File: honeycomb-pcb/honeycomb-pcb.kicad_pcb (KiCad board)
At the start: 4 copper layers, 40 x 40 mm, 103 parts, among them J1301 Connector_USB_C_Receptacle, J301 Molex_Pico-SPOX_Horizontal, J302 Molex_Pico-Lock-PLUS_Vertical, J401 Molex_Pico-SPOX_Horizontal, J402 Molex_Pico-Clasp_Horizontal, M301 Fan_5VDC_25x25x8mm, Q301 MOSFET-N-CH, SW1301 Switch_Tactile_SPST-NO_SMT_Si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, U1001 BUK7D36-60EX, U1101 BUK7D36-60EX, U1201 BUK7D36-60EX, U1301 Linear_3.3V_1A, U1302 MCU_RP2040, U1303 Memory_Flash_W25Q128JVZPIQ, U301 Switching_5V_500mA, U302 Linear_3.3V_1A, U401 TMC5160A-WA, U402 MAX6816, U501 BUK7D36-60EX, U601 BUK7D36-60EX, U701 BUK7D36-60EX, U801 BUK7D36-60EX, U901 BUK7D36-60EX, X401 16MHz, Y1301 Crystal_12MHz

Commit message: tmc5130-uart-multiplexer -> honeycomb-pcb
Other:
- board text added: "honeycomb-pcb v1.0 2024/05 48V 1.6A RMS 2.2A PEAK"
- board text added: "https://github.com/janelia-kicad/honeycomb-pcb"
- board text removed: "https://github.com/janelia-kicad/tmc5130-uart-multiplexer"
- board text removed: "tmc5130-uart-multiplexer v1.0 2024/05 48V 1.6A RMS 2.2A PEAK"
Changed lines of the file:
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@@
   (paper "A4")
   (title_block
-    (title "tmc5130-uart-multiplexer")
+    (title "honeycomb-pcb")
     (date "2024-05-08")
     (rev "1.0")
@@
     (effects (font (size 1 0.6) (thickness 0.15) bold))
   )
-  (gr_text "tmc5130-uart-multiplexer\nv1.0 2024/05\n48V 1.6A RMS 2.2A PEAK" (at 158.4 116.1) (layer "F.SilkS")
+  (gr_text "honeycomb-pcb\nv1.0 2024/05\n48V 1.6A RMS 2.2A PEAK" (at 158.4 116.1) (layer "F.SilkS")
     (effects (font (size 1 0.6) (thickness 0.15) bold))
   )
-  (gr_text "https://github.com/janelia-kicad/tmc5130-uart-multiplexer" (at 152.4 119.6) (layer "F.SilkS")
+  (gr_text "https://github.com/janelia-kicad/honeycomb-pcb" (at 152.4 119.6) (layer "F.SilkS")
     (effects (font (size 1 0.6) (thickness 0.15) bold))
   )

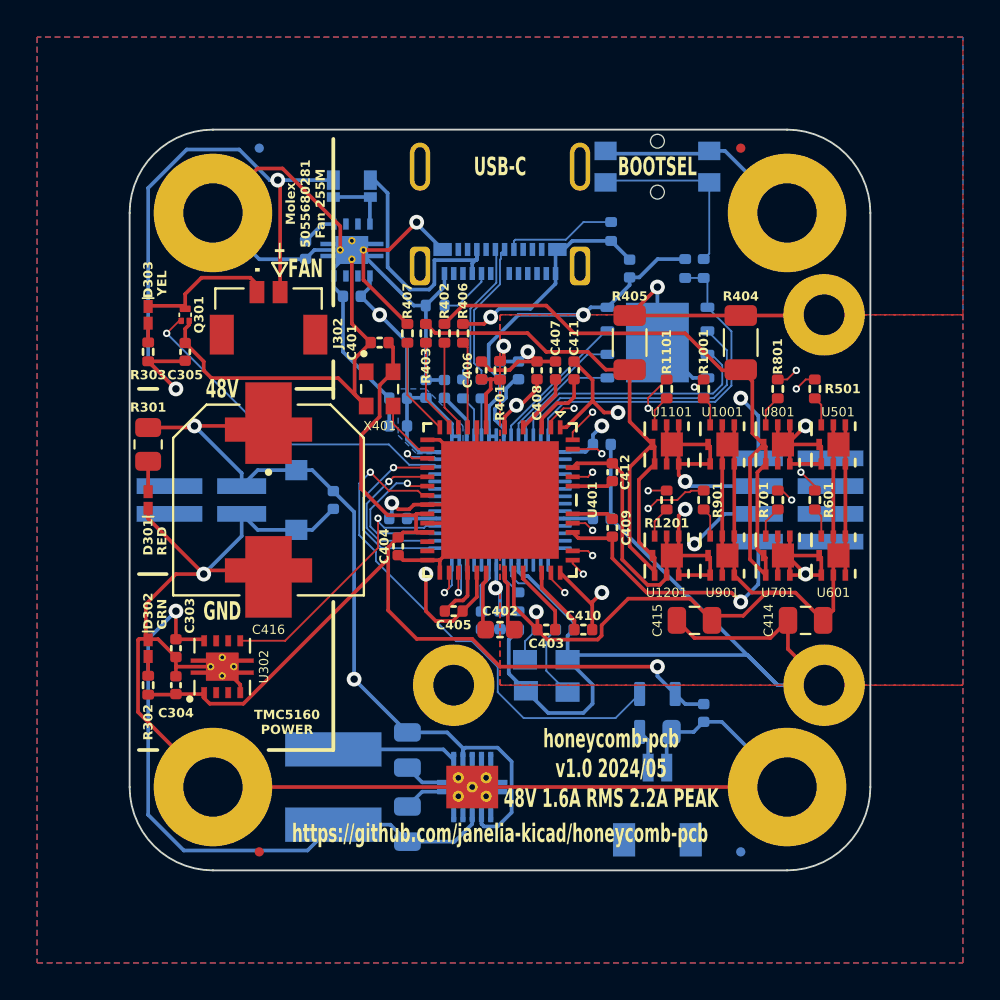
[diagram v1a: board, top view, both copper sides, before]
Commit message: motor -> prism
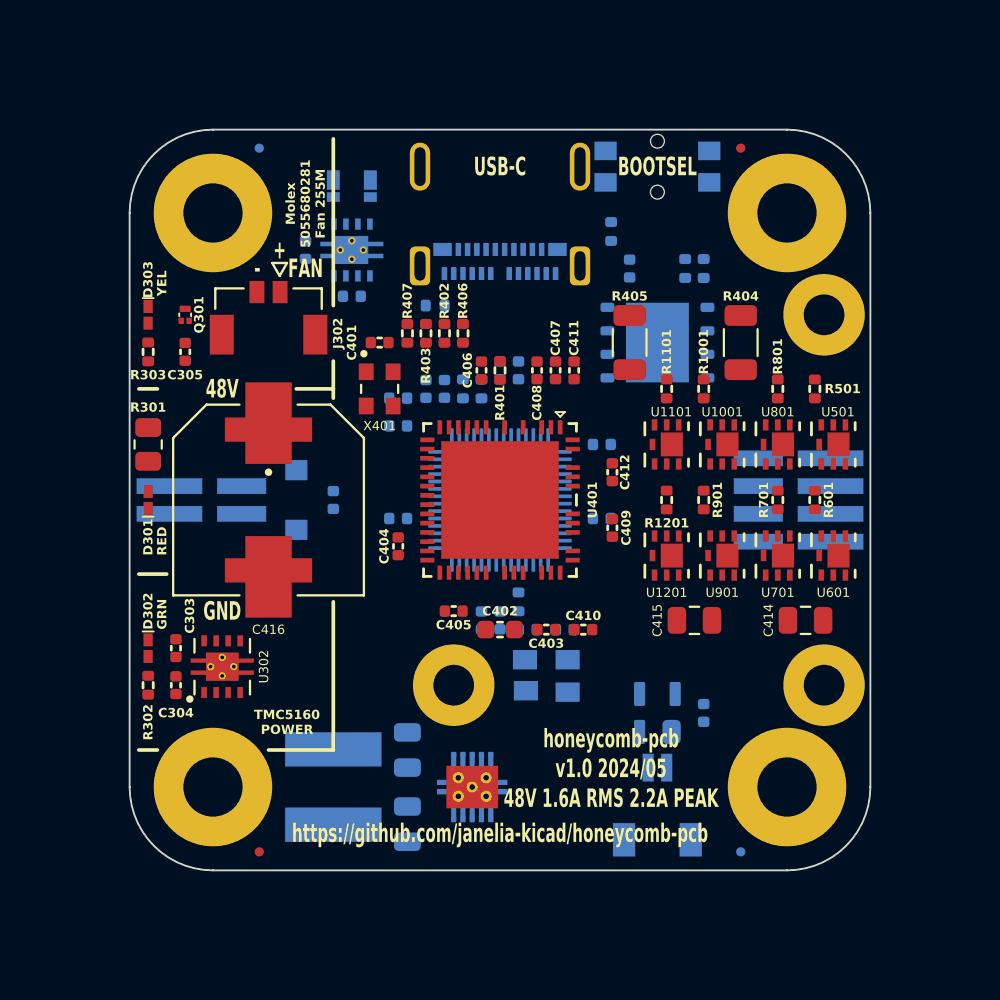
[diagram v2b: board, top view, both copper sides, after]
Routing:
- net /GND: track 474.9 -> 0.00 mm, vias 6 -> 0
- net /VM: track 133.3 -> 0.00 mm, vias 4 -> 0
- net /rp2040/+3.3V: track 87.1 -> 0.00 mm, vias 4 -> 0
- net /+5V: track 81.3 -> 0.00 mm, vias 3 -> 0
- net /VIO: track 56.5 -> 0.00 mm, vias 1 -> 0
- net /tmc5160/BMA1: track 39.3 -> 0.00 mm, vias 2 -> 0
- net /tmc5160/SRA: track 37.6 -> 0.00 mm
- net /tmc5160/BMB2: track 33.1 -> 0.00 mm, vias 2 -> 0
- net /tmc5160/BMA2: track 32.7 -> 0.00 mm, vias 3 -> 0
- net /tmc5160/SRB: track 32.5 -> 0.00 mm
- net /tmc5160/REFL_DEBOUNCED: track 28.1 -> 0.00 mm, vias 1 -> 0
- net /tmc5160/BMB1: track 27.4 -> 0.00 mm, vias 2 -> 0
- net /tmc5160/VCC: track 21.8 -> 0.00 mm, vias 2 -> 0
- net /rp2040/+1.1V: track 20.7 -> 0.00 mm
- net /tmc5160/LA1: track 20.6 -> 0.00 mm, vias 2 -> 0
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- removed copper zone on B.Cu, net /GND
- removed copper zone on F.Cu, net /GND
- removed copper zone on In1.Cu, net /GND
- removed copper zone on F.Cu, net /VM
- removed copper zone on In2.Cu, net /VM
- removed copper zone on B.Cu, net /rp2040/+1.1V
- removed copper zone on B.Cu, net /rp2040/+3.3V

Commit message: Last update before renaming
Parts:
- removed C1301, C1302, C305: 1uF_25V, Janelia:C_0402_1005Metric
- removed C1303, C1311: 1uF_35V, Janelia:C_0402_1005Metric
- removed C1304, C1305, C1306, C1307, C1308, C1309, C1310, C1312, C1313, C1314, C401, C403, C404, C408, C413, C417: 0.1uF_100V, Janelia:C_0402_1005Metric
- removed C1315, C1316: 15pF_25V, Janelia:C_0402_1005Metric
- removed C402: 22nF_100V, Janelia:C_0603_1608Metric
- removed C405: 0.47uF_35V, Janelia:C_0402_1005Metric
- removed C406, C407: 2.2uF_35V, Janelia:C_0402_1005Metric
- removed C409, C410, C411, C412: 0.22uF_25V, Janelia:C_0402_1005Metric
- removed C414, C415: 2.2uF_100V, Janelia:C_0805_2012Metric
- removed C416: 220uF_63V, Janelia:CP_Hybrid_EEHZS1H221V
- removed D1301, D1302: D_SCHOTTKY_40V_2A, Janelia:CR_DSN2_152AB-C_OSI
- removed D302: LED_GRN, Janelia:LED_0402-1005_KNB
- removed D303: LED_YEL, Janelia:LED_0402-1005_KNB
- removed J1301: Connector_USB_C_Receptacle, Janelia:USB_C_Receptacle_Amphenol_10152803-00011LF
- removed J301: Molex_Pico-SPOX_Horizontal, Janelia:Molex_Pico-SPOX-87438_1x02-P1.5mm_Horizontal
- removed J302: Molex_Pico-Lock-PLUS_Vertical, Janelia:Molex_Micro-Lock-PLUS-505568_1x02_P1.25mm_Vertical
- removed J401: Molex_Pico-SPOX_Horizontal, Janelia:Molex_Pico-SPOX-87438_1x04-P1.5mm_Horizontal
- removed J402: Molex_Pico-Clasp_Horizontal, Janelia:Molex_Pico-Clasp-501568_1x02_P1mm_Horizontal
- removed L301: 150uH_553mA, Janelia:IND_CB_SD25
- removed R1201: 15, Janelia:R_0402_1005Metric
- removed R1301: 10.0k, Janelia:R_0402_1005Metric
- removed R1302, R1303: 5.1k, Janelia:R_0402_1005Metric
- removed R1304, R1305: 27, Janelia:R_0402_1005Metric
- removed R1306, R1307: 1k, Janelia:R_0402_1005Metric
- removed R303: 249, Janelia:R_0402_1005Metric
- removed R401: 2.2, Janelia:R_0402_1005Metric
- removed R402, R403, R406, R407: 47, Janelia:R_0402_1005Metric
- removed R404, R405: 0.15, Janelia:R_1206_3216Metric
- removed SW1301: Switch_Tactile_SPST-NO_SMT_Side, Janelia:SMT_1045822_WRE
- removed U1201: BUK7D36-60EX, Janelia:BUK7D3660EX_NEX
- removed U1301, U302: Linear_3.3V_1A, Janelia:TPS737Q1
- removed U1302: MCU_RP2040, Janelia:QFN-56-1EP_7x7mm_P0.4mm_EP3.2x3.2mm
- removed U1303: Memory_Flash_W25Q128JVZPIQ, Janelia:WSON-8-1EP_6x5mm_P1.27mm_EP3.4x4.3mm
- removed U401: TMC5160A-WA, Janelia:21-100593_ADI
- removed U402: MAX6816, Janelia:SOT192P237X122-4N
- removed X401: 16MHz, Janelia:OSC_ECS-2520S33-160-FN-TR
- removed Y1301: Crystal_12MHz, Janelia:Crystal_SMD_Abracon_ABM8-4Pin_3.2x2.5mm
- added A401: PICO_W5500_EVB, Janelia:Pico_Header_Holes, F.Cu at (128.3, 101.6)
- added C1001: 0.1uF_100V, Janelia:C_0402_1005Metric, F.Cu at (377.9, 81.9)
- added C1002: 1uF_35V, Janelia:C_0402_1005Metric, F.Cu at (377.9, 83.8)
- added C1101: 0.1uF_100V, Janelia:C_0402_1005Metric, F.Cu at (377.9, 43.8)
- added C1102: 1uF_35V, Janelia:C_0402_1005Metric, F.Cu at (377.9, 45.8)
- added C501: 0.1uF_100V, Janelia:C_0402_1005Metric, F.Cu at (377.9, 24.8)
- added C502: 1uF_35V, Janelia:C_0402_1005Metric, F.Cu at (377.9, 26.7)
- added C601: 0.1uF_100V, Janelia:C_0402_1005Metric, F.Cu at (377.9, 62.8)
- added C602: 1uF_35V, Janelia:C_0402_1005Metric, F.Cu at (377.9, 64.8)
- added C701: 0.1uF_100V, Janelia:C_0402_1005Metric, F.Cu at (398.0, 43.8)
- added C702: 1uF_35V, Janelia:C_0402_1005Metric, F.Cu at (398.0, 45.8)
- added C801: 0.1uF_100V, Janelia:C_0402_1005Metric, F.Cu at (398.0, 62.8)
- added C802: 1uF_35V, Janelia:C_0402_1005Metric, F.Cu at (398.0, 64.8)
- added C901: 0.1uF_100V, Janelia:C_0402_1005Metric, F.Cu at (398.0, 24.8)
- added C902: 1uF_35V, Janelia:C_0402_1005Metric, F.Cu at (398.0, 26.7)
- added D1001: D, Janelia:D_SMB, F.Cu at (372.3, 79.1)
- added D1002: D_Zener_47V_1W, Janelia:D_SMA, F.Cu at (380.5, 78.6)
- added D1101: D, Janelia:D_SMB, F.Cu at (372.3, 41.0)
- added D1102: D_Zener_47V_1W, Janelia:D_SMA, F.Cu at (380.5, 40.5)
- added D501: D, Janelia:D_SMB, F.Cu at (372.3, 22.0)
- added D502: D_Zener_47V_1W, Janelia:D_SMA, F.Cu at (380.5, 21.5)
- added D601: D, Janelia:D_SMB, F.Cu at (372.3, 60.1)
- added D602: D_Zener_47V_1W, Janelia:D_SMA, F.Cu at (380.5, 59.6)
- added D701: D, Janelia:D_SMB, F.Cu at (392.4, 41.0)
- added D702: D_Zener_47V_1W, Janelia:D_SMA, F.Cu at (400.6, 40.5)
- added D801: D, Janelia:D_SMB, F.Cu at (392.4, 60.1)
- added D802: D_Zener_47V_1W, Janelia:D_SMA, F.Cu at (400.6, 59.6)
- added D901: D, Janelia:D_SMB, F.Cu at (392.4, 22.0)
- added D902: D_Zener_47V_1W, Janelia:D_SMA, F.Cu at (400.6, 21.5)
- added J1001: FFC_P1mm_BOT_RA_SMD, Janelia:CONN_C2914097, F.Cu at (377.2, 75.1)
- added J1101: FFC_P1mm_BOT_RA_SMD, Janelia:CONN_C2914097, F.Cu at (377.2, 37.0)
- added J501: FFC_P1mm_BOT_RA_SMD, Janelia:CONN_C2914097, F.Cu at (172.4, 71.6)
- added J601: FFC_P1mm_BOT_RA_SMD, Janelia:CONN_C2914097, F.Cu at (377.2, 56.0)
- added J701: FFC_P1mm_BOT_RA_SMD, Janelia:CONN_C2914097, F.Cu at (397.3, 37.0)
- added J801: FFC_P1mm_BOT_RA_SMD, Janelia:CONN_C2914097, F.Cu at (397.3, 56.0)
- added J901: FFC_P1mm_BOT_RA_SMD, Janelia:CONN_C2914097, F.Cu at (397.3, 17.9)
- added Q302: MOSFET-N-CH-EN_100V_260mA, Janelia:SOT-23, F.Cu at (346.1, 81.5)
- added R1002: 100, Janelia:R_0402_1005Metric, F.Cu at (380.8, 81.9)
- added R1102: 100, Janelia:R_0402_1005Metric, F.Cu at (380.8, 43.8)
- added R502: 100, Janelia:R_0402_1005Metric, F.Cu at (380.8, 24.8)
- added R602: 100, Janelia:R_0402_1005Metric, F.Cu at (380.8, 62.9)
- added R702: 100, Janelia:R_0402_1005Metric, F.Cu at (400.9, 43.8)
- added R802: 100, Janelia:R_0402_1005Metric, F.Cu at (400.9, 62.9)
- added R902: 100, Janelia:R_0402_1005Metric, F.Cu at (400.9, 24.8)
- added T301: TERM_BLK_HDR_2POS_90DEG_0.2IN, Janelia:PHOENIX_1757242, F.Cu at (345.0, 78.3)
- C301: value 2.2uF_100V -> 3.3uF_50V; footprint Janelia:C_0805_2012Metric -> Janelia:C_1210_3225Metric
- C302: value 47uF_10V -> 0.1uF_100V; footprint Janelia:C_0805_2012Metric -> Janelia:C_0402_1005Metric
- D301: value LED_RED -> D_50V_15A; footprint Janelia:LED_0402-1005_KNB -> Janelia:POWERDI5_DIO
- D401: value D_Zener_48V_2.6A -> D_SCHOTTKY_20V_1A; footprint Janelia:SMFSeries_LTF -> Janelia:DIOM3616X98N
- Q301: value MOSFET-N-CH -> MOSFET-P-CH-EN_60V_50A; footprint Janelia:XFDFN-3 -> Janelia:TO-252-2
- R1001, R1101, R501, R601, R701, R801, R901: value 15 -> 0.24; footprint Janelia:R_0402_1005Metric -> Janelia:R_2512_6332Metric
- R301: value 2.32k -> 1k; footprint Janelia:R_0805_2012Metric -> Janelia:R_0402_1005Metric
- R302: value 64.9 -> 3.6k
- U1001, U1101, U501, U601, U701, U801, U901: value BUK7D36-60EX -> MAX13431E; footprint Janelia:BUK7D3660EX_NEX -> Janelia:21-0137I_T1033-1_MXM
- U301: value Switching_5V_500mA -> TPSM365R6V5RDNR; footprint Janelia:Texas_S-PVSON-N10_ThermalVias -> Janelia:RDN0011A-MFG
- moved R701 413.0 mm to (554.4, 245.8)
- moved U1101 406.5 mm to (555.6, 197.6)
- moved R801 394.1 mm to (542.6, 216.1)
- moved R901 384.4 mm to (522.1, 239.6)
- moved R301 378.2 mm to (510.1, 65.3)
- moved R1001 377.9 mm to (530.4, 185.6)
- moved C301 365.3 mm to (512.6, 111.8)
- moved R1101 362.4 mm to (513.9, 179.6)
- moved D301 360.1 mm to (492.4, 74.1)
- moved Q301 356.8 mm to (490.1, 52.3)
- moved R302 352.8 mm to (484.6, 78.6)
- moved C303 350.3 mm to (482.1, 63.9)
- moved D401 350.1 mm to (491.4, 91.6)
- moved C304 337.5 mm to (471.6, 88.6)
- moved M301 325.8 mm to (484.4, 131.1)
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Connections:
- C301 pad 1: /VM -> /power/VBB
- C302 pad 1: /+5V -> /power/VBB
- C303 pad 1: /+5V -> /VCC
- C304 pad 1: /VIO -> /+5V
- D301 pad 1: /GND -> /power/VBB
- D301 pad 2: /power/LED_RED+ -> /power/VAA
- D401 pad 1: /VM -> /microcontroller/VSYS
- D401 pad 2: /GND -> /+5V
- M301 pad 1: /GND -> /+5V
- Q301 pad 1: /ENABLE_FAN -> /power/~{ENABLE_VCC}
- Q301 pad 2: /GND -> /VCC
- Q301 pad 3: /power/FAN- -> /power/VBB
- R1001 pad 1: /tmc5160/HB1 -> /VCC
- R1001 pad 2: /tmc5160/mosfet5/GATEB -> /prism4/VBB
- R1101 pad 1: /tmc5160/LB1 -> /VCC
- R1101 pad 2: /tmc5160/mosfet7/GATEB -> /prism6/VBB
- R301 pad 1: /VM -> /power/VBB
- R301 pad 2: /power/LED_RED+ -> /power/~{ENABLE_VCC}
- R302 pad 1: /VIO -> /power/~{ENABLE_VCC}
- R302 pad 2: /power/LED_GRN+ -> Net-(Q302-D)
- R501 pad 1: /tmc5160/HA1 -> /VCC
- R501 pad 2: /tmc5160/mosfet1/GATEB -> /prism0/VBB
- R601 pad 1: /tmc5160/HA2 -> /VCC
- R601 pad 2: /tmc5160/mosfet2/GATEB -> /prism1/VBB
- R701 pad 1: /tmc5160/LA2 -> /VCC
- R701 pad 2: /tmc5160/mosfet4/GATEB -> /prism2/VBB
- R801 pad 1: /tmc5160/LA1 -> /VCC
- R801 pad 2: /tmc5160/mosfet3/GATEB -> /prism3/VBB
- R901 pad 1: /tmc5160/HB2 -> /VCC
- R901 pad 2: /tmc5160/mosfet6/GATEB -> /prism5/VBB
- U1001 pad 1: /VM -> /+3.3V
- U1001 pad 2: /VM -> /RX
- U1001 pad 3: /tmc5160/mosfet5/GATEB -> /ENABLE_TX_4
- U1001 pad 4: /tmc5160/BMB1 -> /~{ENABLE_RX_4}
- U1001 pad 5: /VM -> /TX
- U1001 pad 6: /VM -> /GND
- U1001 pad 7: /VM -> (no net)
- U1001 pad 8: /tmc5160/BMB1 -> /prism4/SWP
- U1101 pad 1: /tmc5160/BMB1 -> /+3.3V
- U1101 pad 2: /tmc5160/BMB1 -> /RX
- U1101 pad 3: /tmc5160/mosfet7/GATEB -> /ENABLE_TX_6
- U1101 pad 4: /tmc5160/SRB -> /~{ENABLE_RX_6}
- U1101 pad 5: /tmc5160/BMB1 -> /TX
- U1101 pad 6: /tmc5160/BMB1 -> /GND
- U1101 pad 7: /tmc5160/BMB1 -> (no net)
- U1101 pad 8: /tmc5160/SRB -> /prism6/SWP
- U301 pad 1: /power/SW -> unconnected-(U301-PGOOD-Pad1)
- U301 pad 11: /GND -> /VCC
- U301 pad 2: /VM -> /power/VBB
- U301 pad 3: /GND -> /power/VBB
- U301 pad 4: unconnected-(U301-SS-Pad4) -> /+5V
- U301 pad 5: /GND -> unconnected-(U301-SW-Pad5)
- U301 pad 7: /VM -> unconnected-(U301-BOOT-Pad7)
- U301 pad 8: /+5V -> /VCC
- U301 pad 9: unconnected-(U301-HYS-Pad9) -> /+5V
- U501 pad 1: /VM -> /+3.3V
- U501 pad 2: /VM -> /RX
- U501 pad 3: /tmc5160/mosfet1/GATEB -> /ENABLE_TX_0
- U501 pad 4: /tmc5160/BMA1 -> /~{ENABLE_RX_0}
- U501 pad 5: /VM -> /TX
- U501 pad 6: /VM -> /GND
- U501 pad 7: /VM -> (no net)
- U501 pad 8: /tmc5160/BMA1 -> /prism0/SWP
- U601 pad 1: /VM -> /+3.3V
- U601 pad 2: /VM -> /RX
- U601 pad 3: /tmc5160/mosfet2/GATEB -> /ENABLE_TX_1
- U601 pad 4: /tmc5160/BMA2 -> /~{ENABLE_RX_1}
- U601 pad 5: /VM -> /TX
- U601 pad 6: /VM -> /GND
- U601 pad 7: /VM -> (no net)
- U601 pad 8: /tmc5160/BMA2 -> /prism1/SWP
- U701 pad 1: /tmc5160/BMA2 -> /+3.3V
- U701 pad 2: /tmc5160/BMA2 -> /RX
- U701 pad 3: /tmc5160/mosfet4/GATEB -> /ENABLE_TX_2
- U701 pad 4: /tmc5160/SRA -> /~{ENABLE_RX_2}
- U701 pad 5: /tmc5160/BMA2 -> /TX
- U701 pad 6: /tmc5160/BMA2 -> /GND
- U701 pad 7: /tmc5160/BMA2 -> (no net)
- U701 pad 8: /tmc5160/SRA -> /prism2/SWP
- U801 pad 1: /tmc5160/BMA1 -> /+3.3V
- U801 pad 2: /tmc5160/BMA1 -> /RX
- U801 pad 3: /tmc5160/mosfet3/GATEB -> /ENABLE_TX_3
- U801 pad 4: /tmc5160/SRA -> /~{ENABLE_RX_3}
- U801 pad 5: /tmc5160/BMA1 -> /TX
- U801 pad 6: /tmc5160/BMA1 -> /GND
- U801 pad 7: /tmc5160/BMA1 -> (no net)
- U801 pad 8: /tmc5160/SRA -> /prism3/SWP
- U901 pad 1: /VM -> /+3.3V
- U901 pad 2: /VM -> /RX
- U901 pad 3: /tmc5160/mosfet6/GATEB -> /ENABLE_TX_5
- U901 pad 4: /tmc5160/BMB2 -> /~{ENABLE_RX_5}
- U901 pad 5: /VM -> /TX
- U901 pad 6: /VM -> /GND
- U901 pad 7: /VM -> (no net)
- U901 pad 8: /tmc5160/BMB2 -> /prism5/SWP
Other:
- board text removed: "+"
- board text removed: "-"
- board text removed: "48V"
- board text removed: "A1"
- board text removed: "A2"
- board text removed: "B1"
- board text removed: "B2"
- board text removed: "BOOTSEL"
- board text removed: "FAN"
- board text removed: "GND"
- board text removed: "GRN"
- board text removed: "Molex 0874380243"
- board text removed: "Molex 0874380443"
- board text removed: "Molex 5015680207"
- board text removed: "Molex 5055680281 Fan 255M"
- board text removed: "RED"
- board text removed: "REFL"
- board text removed: "TMC5160 POWER"
- board text removed: "USB-C"
- board text removed: "YEL"
- board text removed: "honeycomb-pcb v1.0 2024/05 48V 1.6A RMS 2.2A PEAK"
- board text removed: "https://github.com/janelia-kicad/honeycomb-pcb"
